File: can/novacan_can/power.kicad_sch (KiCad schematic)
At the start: 28 parts, among them J1 USB_C_Receptacle_USB2.0_14P, Q1 FS8205A, U1 DW01A, U2 USBLC6-2SC6, U3 TPS63020DSJR, U4 MP28163GQ-P

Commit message: added pdf
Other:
- company, title: (none) -> NovaGlider
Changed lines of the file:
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@@
 	(generator_version "9.0")
 	(paper "A4")
+	(title_block
+		(title "NovaGlider")
+		(date "2025-12-02")
+		(rev "v1.0")
+		(company "NovaGlider")
+		(comment 1 "part of Saint-Barbara college")
+		(comment 2 "created by Sam Vandenabeele")
+	)
 	(junction
 		(at 48.26 106.68)

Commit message: bugfixes + schematic.pdf
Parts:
- added C24, C25: 10uF, symbol Device:C
- added D1, D2: LED, symbol Device:LED
- added R16: 1.2K, symbol Device:R
- added R17: 47k, symbol Device:R
- added R18: 4.7k, symbol Device:R
- added R19: 0.4, symbol Device:R
- added SW5: SW_SPDT, symbol Switch:SW_SPDT
- added TH1: Therm_NTC, symbol Device:Thermistor_NTC
- added U9: TP4056-42-ESOP8, Package_SO:SOIC-8-1EP_3.9x4.9mm_P1.27mm_EP2.41x3.3mm_ThermalVias, symbol Battery_Management:TP4056-42-ESOP8
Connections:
- net +BATT: now also C24.1, U9.5 (BAT)
- net -BATT: now also C2.1, C3.1, C4.2, C5.1, C6.1, C7.1, C9.1, J1.A1 (GND), J1.A12 (GND), J1.B1 (GND), J1.B12 (GND), J1.S1 (SHIELD), R3.2, R4.2, R6.2, R9.2, U2.5 (VBUS), U3.15 (PGND), U3.2 (GND), U4.3 (PGND), U4.9 (AGND), C24.2, C25.2, R16.2, R17.2, TH1.1, U9.3 (GND), U9.9 (EPAD)
- net VBUS: now reaches J1.A4 (VBUS), J1.A9 (VBUS), J1.B4 (VBUS), J1.B9 (VBUS), U2.2 (GND)
- net VBUS: now also R19.1
- removed net GND: BT1.2 (-), C1.2, C2.1, C3.1, C4.2, C5.1, C6.1, C7.1, C9.1, J1.A1 (GND), J1.A12 (GND), J1.B1 (GND), J1.B12 (GND), J1.S1 (SHIELD), Q1.2, Q1.3, R3.2, R4.2, R6.2, R9.2, U1.6 (GND), U2.5 (VBUS), U3.15 (PGND), U3.2 (GND), U4.3 (PGND), U4.9 (AGND)
- new net: R17.1, R18.2, TH1.2, U9.1 (TEMP)
- new net: BT1.2 (-), SW5.3 (C)
- new net: C25.1, D1.2 (A), D2.2 (A), R18.1, R19.2, U9.4 (V_{CC}), U9.8 (CE)
- new net: C1.2, Q1.2, Q1.3, SW5.2 (B), U1.6 (GND)
- new net: D2.1 (K), U9.6 (~{STDBY})
- new net: R16.1, U9.2 (PROG)
- new net: D1.1 (K), U9.7 (~{CHRG})
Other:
- moved on the sheet: C9, U2

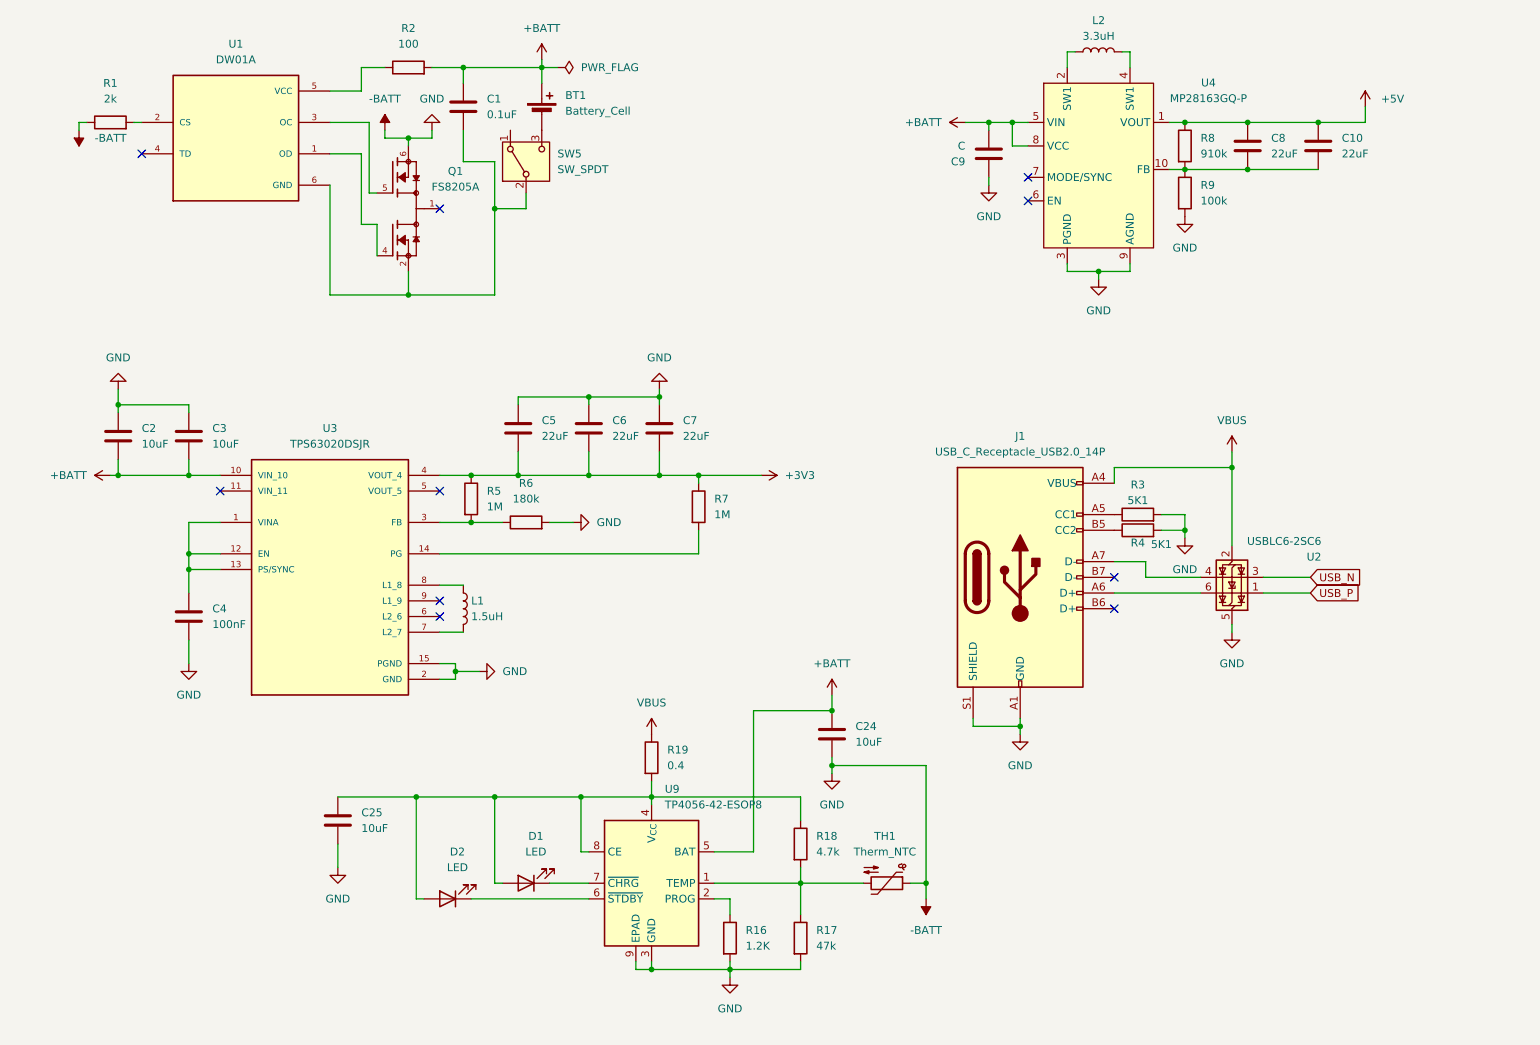
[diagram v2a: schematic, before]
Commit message: added footprints and symbols, changed issues pointed out by reddit users' review
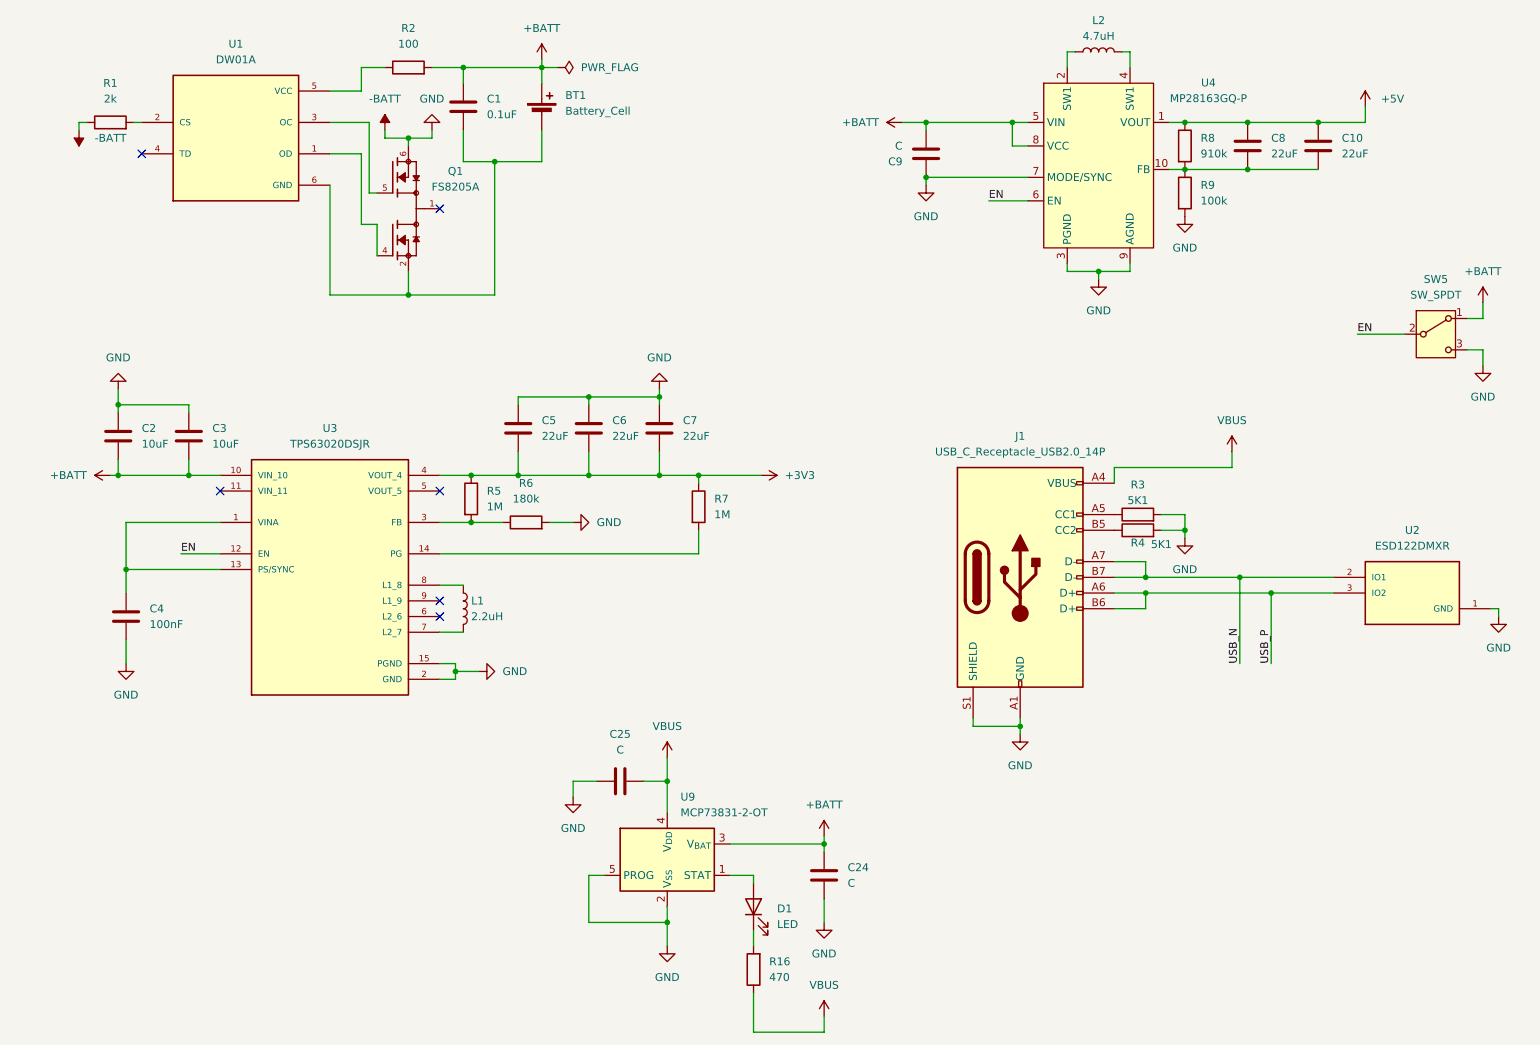
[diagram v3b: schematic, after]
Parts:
- removed D2: LED, symbol Device:LED
- removed R17: 47k, symbol Device:R
- removed R18: 4.7k, symbol Device:R
- removed R19: 0.4, symbol Device:R
- removed TH1: Therm_NTC, symbol Device:Thermistor_NTC
- removed U2: USBLC6-2SC6, Package_TO_SOT_SMD:SOT-23-6, symbol Power_Protection:USBLC6-2SC6
- removed U9: TP4056-42-ESOP8, Package_SO:SOIC-8-1EP_3.9x4.9mm_P1.27mm_EP2.41x3.3mm_ThermalVias, symbol Battery_Management:TP4056-42-ESOP8
- added U2: ESD122DMXR, ESD122DMXR:IC_ESD122DMXR, symbol ESD122DMXR:ESD122DMXR
- added U9: MCP73831-2-OT, Package_TO_SOT_SMD:SOT-23-5, symbol Battery_Management:MCP73831-2-OT
- C24, C25: value 10uF -> C
- L1: value 1.5uH -> 2.2uH
- L2: value 3.3uH -> 4.7uH
- R16: value 1.2K -> 470
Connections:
- net +BATT: now also SW5.1 (A), U9.3 (V_{BAT})
- net -BATT: now also SW5.3 (C), U4.7 (MODE/SYNC), U2.1 (GND), U9.2 (V_{SS}), U9.5 (PROG); no longer R16.2
- net USB_N: now also J1.A7 (D-), J1.B7 (D-), U2.2 (IO1)
- net USB_P: now also J1.A6 (D+), J1.B6 (D+), U2.3 (IO2)
- net VBUS: now also C25.1, R16.1, U9.4 (V_{DD})
- net at BT1.2 (-): now also C1.2, Q1.2, Q1.3, U1.6 (GND); no longer SW5.3 (C)
- net at D1.2 (A): now also U9.1 (STAT); no longer C25.1
- net at C4.1, U3.1 (VINA), U3.13 (PS/SYNC): no longer U3.12 (EN)
- net EN: now reaches U4.6 (EN)
- net EN: now also SW5.2 (B), U3.12 (EN)
- net at D1.1 (K): now also R16.2
- no-connect marks 10 -> 6
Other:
- moved on the sheet: C4, C9

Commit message: added extra footprints, resolved ESD issues
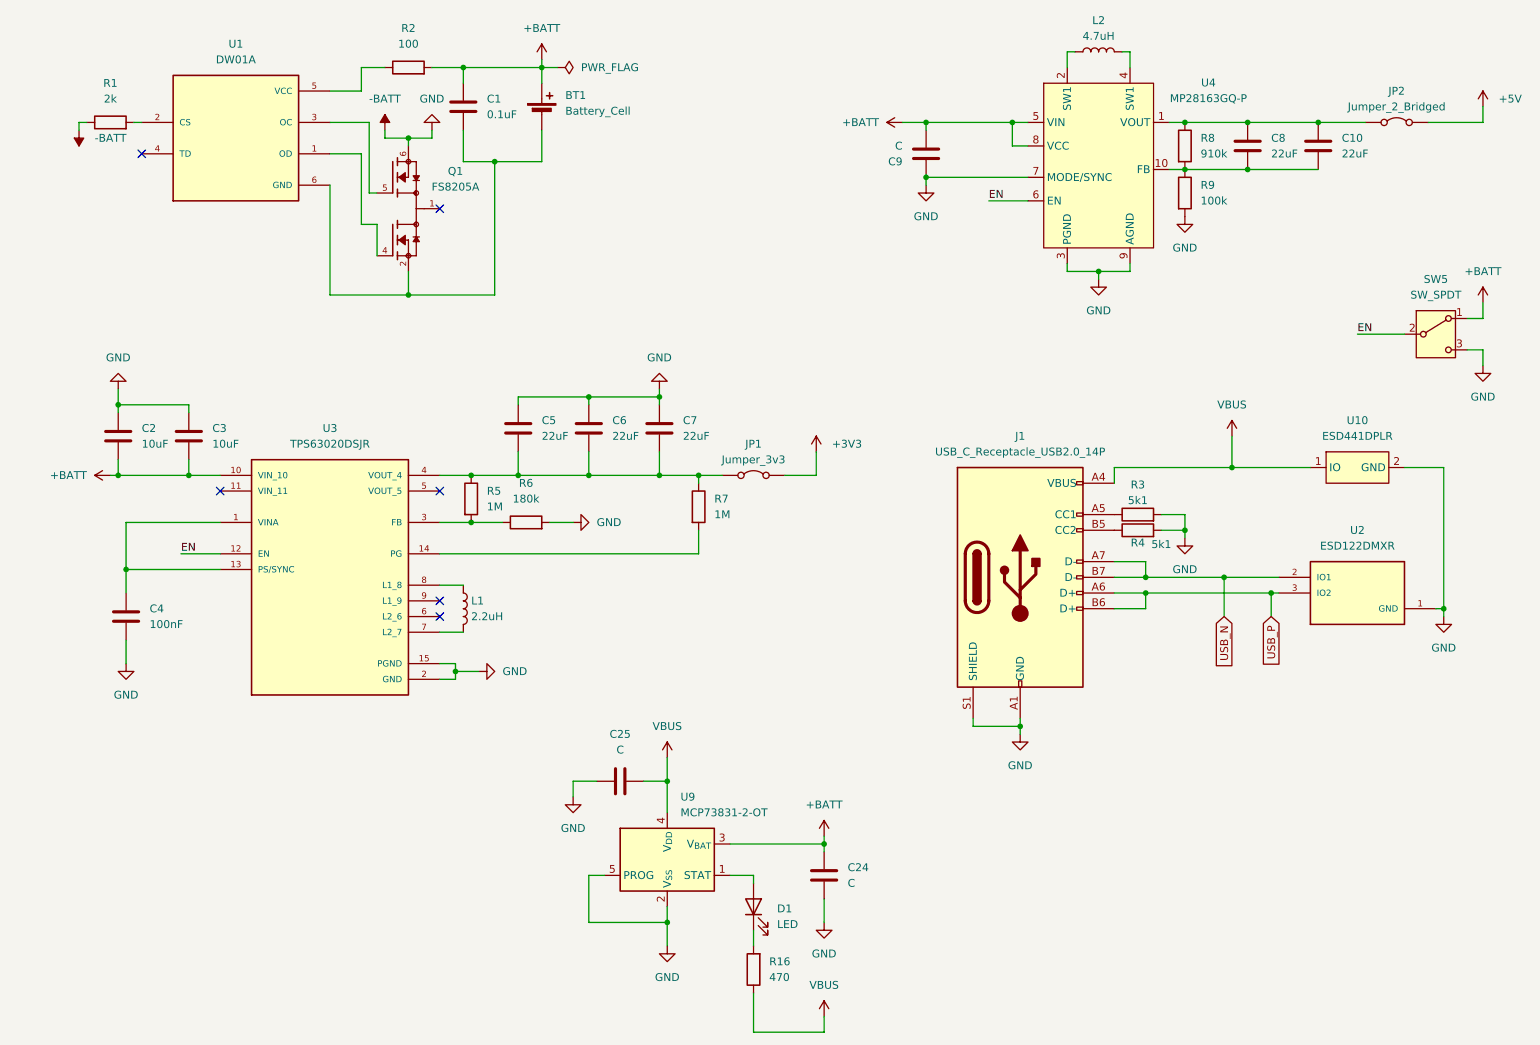
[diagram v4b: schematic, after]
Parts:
- added JP1: Jumper_3v3, symbol Jumper:Jumper_2_Bridged
- added JP2: Jumper_2_Bridged, symbol Jumper:Jumper_2_Bridged
- added U10: ESD441DPLR, ESD441DPLR:DIODFN60X30X32-2N, symbol ESD441DPLR:ESD441DPLR
- R3, R4: value 5K1 -> 5k1
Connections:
- net +3V3: now also JP1.2 (B); no longer C5.2, C6.2, C7.2, R5.1, R7.1, U3.4 (VOUT_4)
- net +5V: now also JP2.2 (B); no longer C10.1, C8.1, R8.1, U4.1 (VOUT)
- net -BATT: now also U10.2 (GND)
- net VBUS: now also U10.1 (IO)
- new net: C10.1, C8.1, JP2.1 (A), R8.1, U4.1 (VOUT)
- new net: C5.2, C6.2, C7.2, JP1.1 (A), R5.1, R7.1, U3.4 (VOUT_4)
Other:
- moved on the sheet: U2
